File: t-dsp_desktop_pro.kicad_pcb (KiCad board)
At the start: 8 copper layers, 120 x 100 mm, 139 parts, among them IC1 Logic Level Shifter - 74HCT2G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, J1 jumper, J10 JST-XH Connector -, J11 JST-XH Connector -, J12 RGB LED HEADEER, J13 Conn_01x02, J15 Conn_01x01, J16 Conn_01x02, J17 Conn_02x04_Odd_Even, J18 Conn_02x02_Odd_Even, J2 GROUND HEADER, J3 jumper, J4 jumper, J5 jumper, J6 jumper, J7 jumper, J8 PJRAS2X1S01X, J9 PJRAS2X1S01X, T108 Tab, T109 Tab, T110 Tab, T111 Tab, U1 Teensy 4.1 - DEVKIT, U2 ESP32-DevKitC - DEVKIT, U3 Power Mux & Protect - TPS2116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, U4 Optoisolators - H11L1SM - 6-S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, U5 Dual Buffer - SN74LVC2G125DCTR, U6 Dual Buffer - SN74LVC2G125DCTR, U7 Dual Buffer - SN74LVC2G125DCTR, U8 Dual Buffer - SN74LVC2G125DCTR, U9 Dual Buffer - 74HCT2G17GW,125

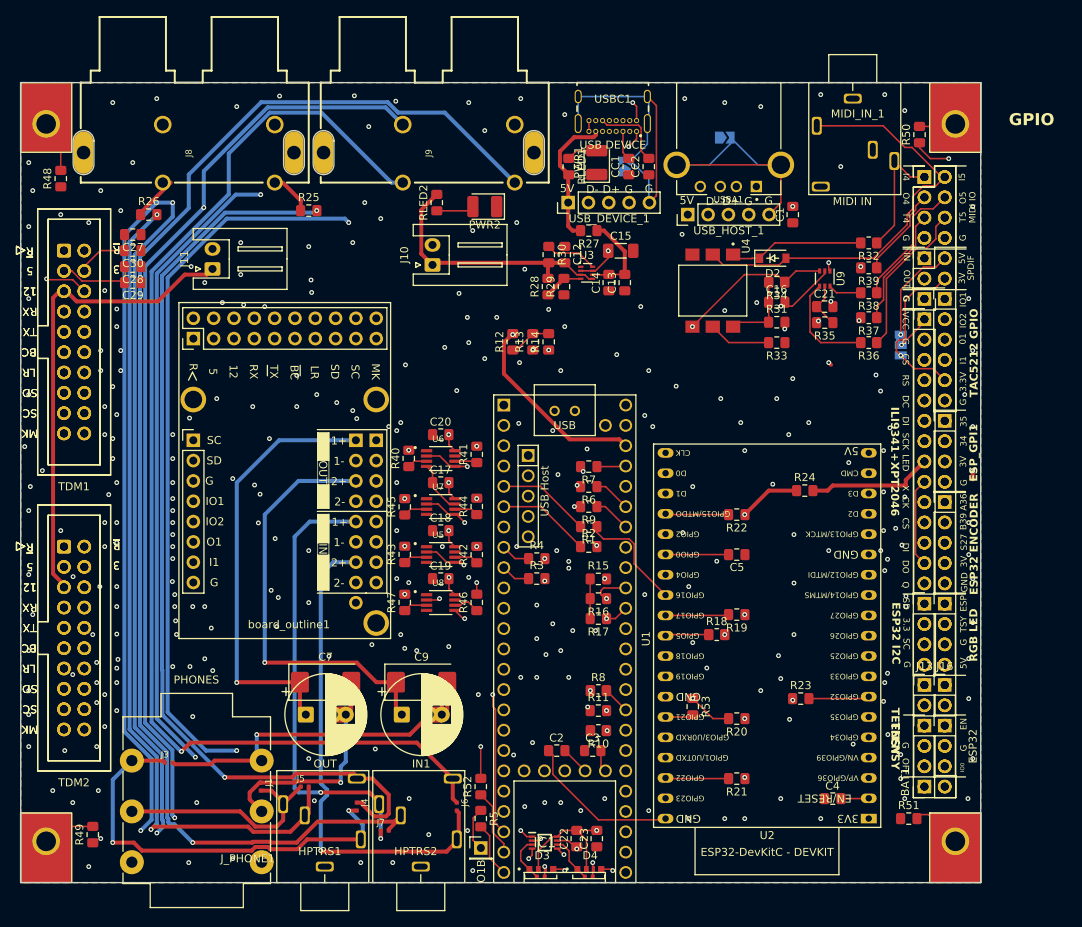
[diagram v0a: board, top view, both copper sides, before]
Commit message: Localize all 3D model paths for Docker/CI rendering
Rewrite all 3D model references from system variables (KICAD9_3DMODEL_DIR,
KISYS3DMOD, KICAD6/8_3DMODEL_DIR) to ${KIPRJMOD}/3d_models/ so models
resolve correctly in Docker-based KiBot CI builds. Copy 45 standard KiCad
3D models to the project. Fix BOM field mismatches for RLED1/RLED2 and
R36/R39 grouping. Update schematic symbol library and footprint libraries.

Co-Authored-By: Claude Opus 4.6 <noreply@anthropic.com>
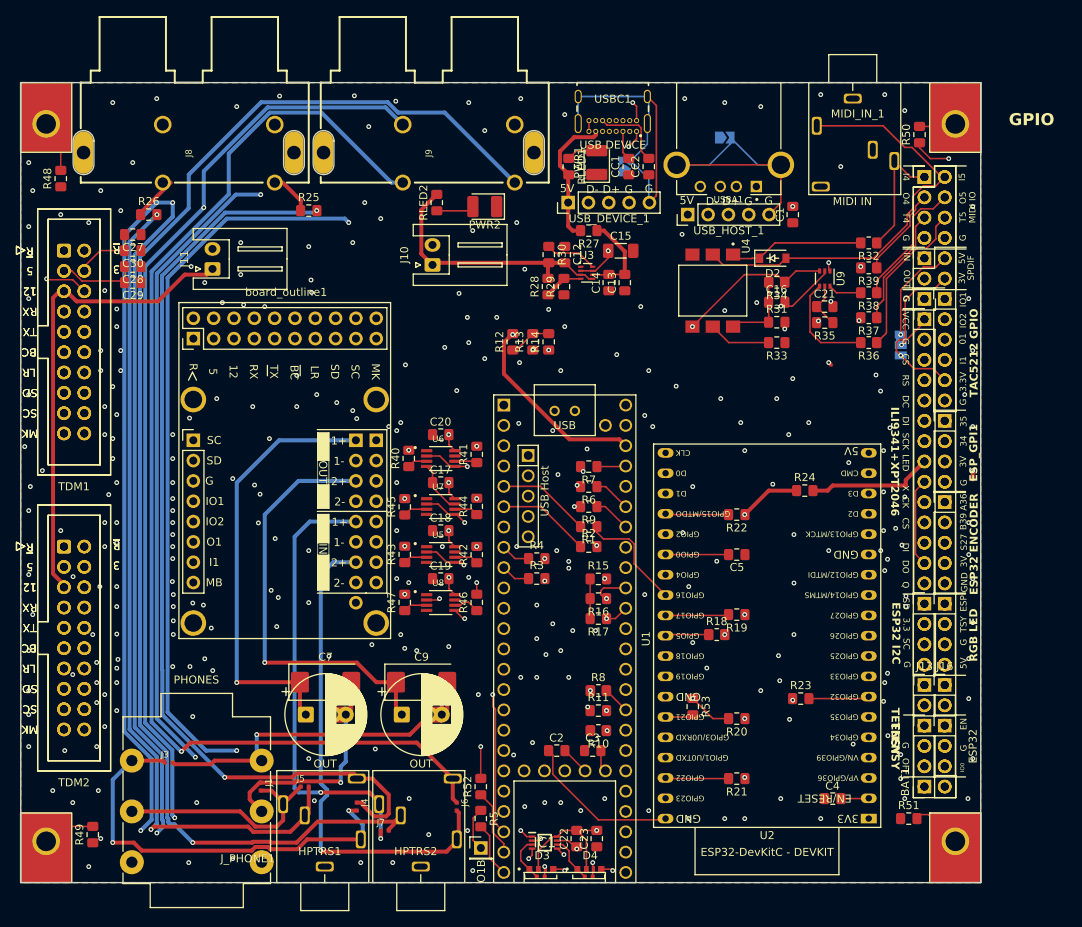
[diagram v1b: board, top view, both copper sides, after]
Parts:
- board_outline1: footprint project_fp:audio_module_board_outline_50x34.5_d1_mod -> project_fp:audio_module_board_outline_50x34.5_d1
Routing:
- net T_BUTTON1: track 63.8 -> 64.9 mm
- net V_BAT: track 53.3 -> 54.1 mm
- net ESP32_IO0: track 90.0 -> 89.3 mm
- net 6_OUT1D+: track 44.3 -> 45.1 mm
- net ESP32_IO14_SPI_SCK: track 45.1 -> 45.8 mm
- net ESP32_IO12_SPI_MISO: track 63.2 -> 63.7 mm
- net TRX3: track 62.7 -> 63.3 mm
